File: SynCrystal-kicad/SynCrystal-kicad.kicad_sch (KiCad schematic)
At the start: 34 parts, among them Q1 BC847, SW1 SW_Push, SW2 SW_Push, U1 NCS20071, U2 74HC14, U3 MCP4725, U4 LMC6482, U5 LMC6482, U6 FSA3157L6X

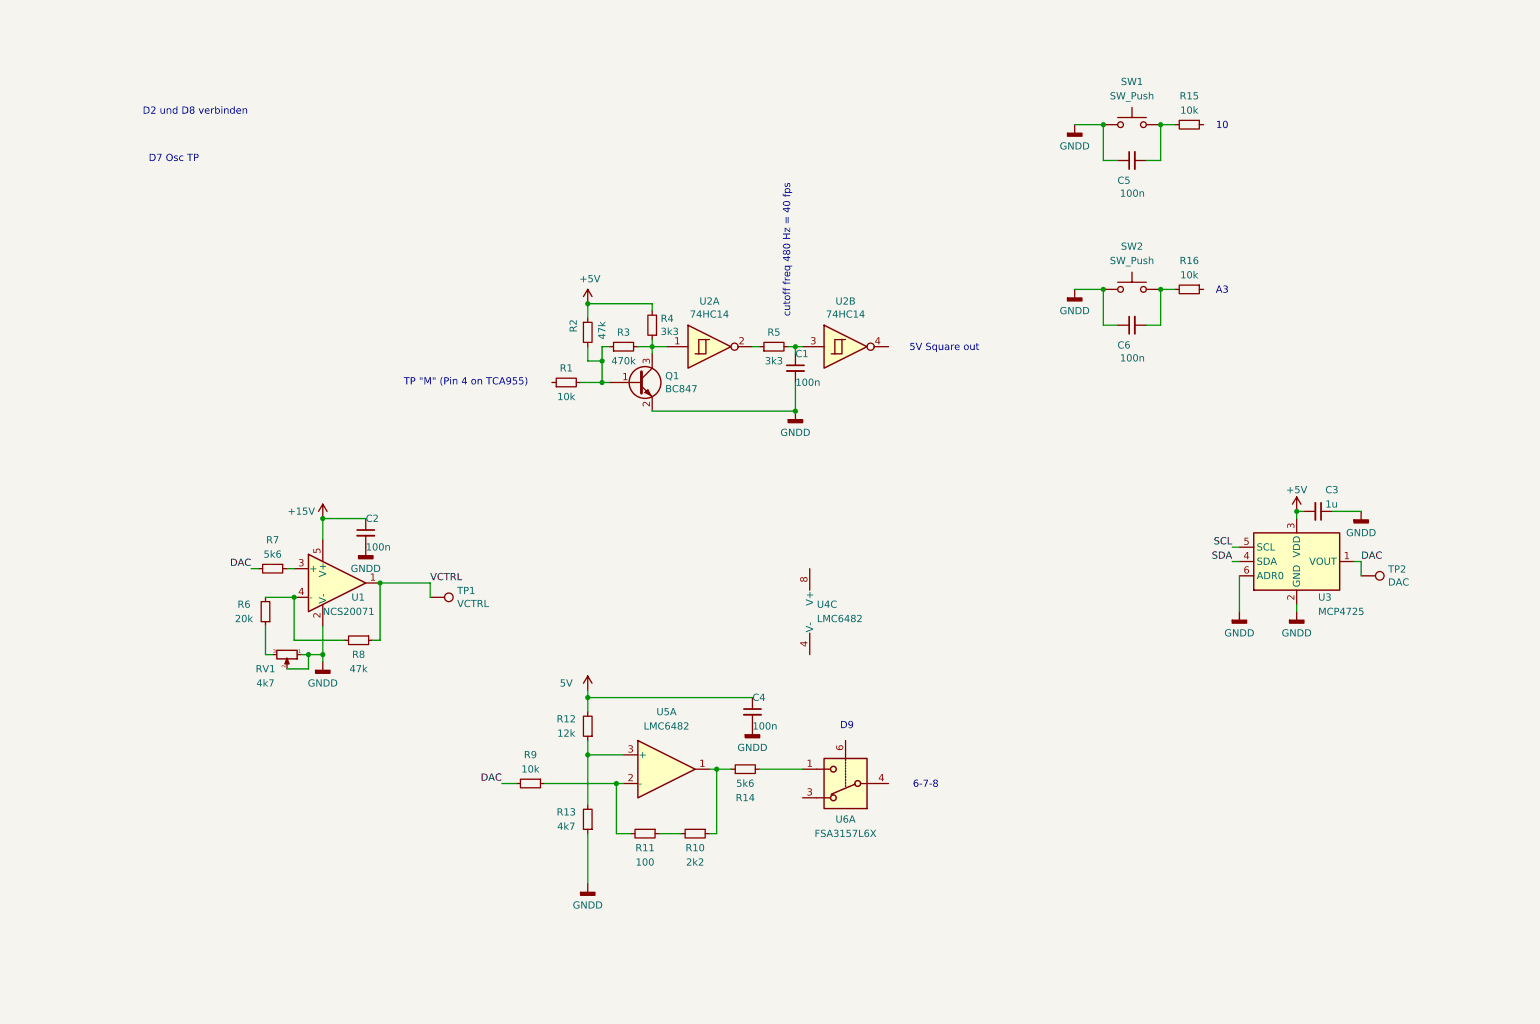
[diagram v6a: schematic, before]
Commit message: pulling the schamtice together
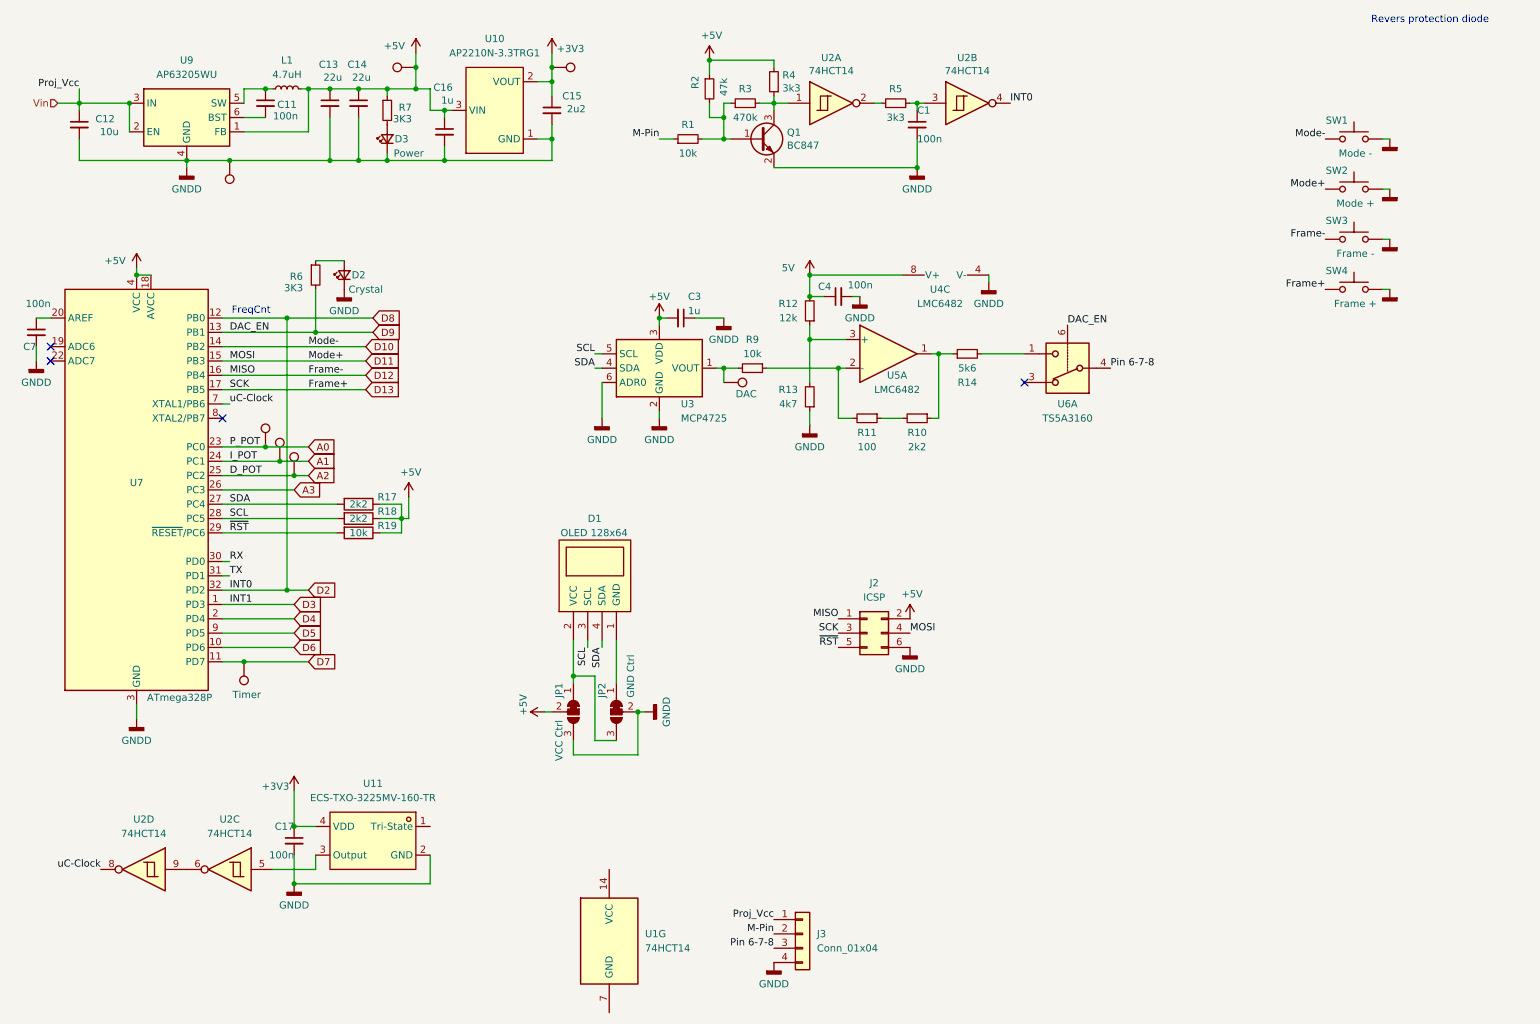
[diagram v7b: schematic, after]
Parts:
- removed C2, C5, C6: 100n, Capacitor_SMD:C_0805_2012Metric, symbol Device:C_Small
- removed R15, R16: 10k, Resistor_SMD:R_0805_2012Metric, symbol Device:R_Small
- removed R8: 47k, Resistor_SMD:R_0805_2012Metric, symbol Device:R_Small
- removed RV1: 4k7, Potentiometer_THT:Potentiometer_Bourns_3296W_Vertical, symbol Device:R_POT_Small
- removed TP1: VCTRL, TestPoint:TestPoint_THTPad_1.5x1.5mm_Drill0.7mm, symbol Connector:TestPoint
- removed TP2: DAC, TestPoint:TestPoint_THTPad_1.5x1.5mm_Drill0.7mm, symbol Connector:TestPoint
- removed U1: NCS20071, Package_TO_SOT_SMD:TSOT-23-5, symbol ErnoCCC-rescue:NCS20071-Amplifier_Operational
- added C11, C17, C7: 100n, Capacitor_SMD:C_0805_2012Metric, symbol Device:C_Small
- added C12: 10u, Capacitor_SMD:C_0805_2012Metric, symbol Device:C_Small
- added C13, C14: 22u, Capacitor_SMD:C_0805_2012Metric, symbol Device:C_Small
- added C15: 2u2, Capacitor_SMD:C_0805_2012Metric, symbol Device:C_Small
- added C16: 1u, Capacitor_SMD:C_0805_2012Metric, symbol Device:C_Small
- added D1: OLED 128x64, Connector_PinHeader_2.54mm:PinHeader_1x04_P2.54mm_Horizontal_shorter, symbol Peacemans Teile:OLED-128-64-I2C-Display_Character
- added D2: Crystal, LED_SMD:LED_0805_2012Metric, symbol Device:LED_Small
- added D3: Power, LED_SMD:LED_0805_2012Metric, symbol Device:LED_Small
- added J2: ICSP, symbol Connector_Generic:Conn_02x03_Odd_Even
- added J3: Conn_01x04, symbol Connector_Generic:Conn_01x04
- added JP1: VCC Ctrl, Jumper:SolderJumper-3_P1.3mm_Bridged12_RoundedPad1.0x1.5mm, symbol Jumper:SolderJumper_3_Bridged12
- added JP2: GND Ctrl, Jumper:SolderJumper-3_P1.3mm_Bridged12_RoundedPad1.0x1.5mm, symbol Jumper:SolderJumper_3_Bridged12
- added L1: 4.7uH, symbol Device:L_Small
- added R17, R18: 2k2, Resistor_SMD:R_0805_2012Metric, symbol Device:R
- added R19: 10k, Resistor_SMD:R_0805_2012Metric, symbol Device:R
- added SW3: Frame -, symbol Switch:SW_Push
- added SW4: Frame +, symbol Switch:SW_Push
- added TP1: P, Peacemans_Footprints:TestPoint_THTPad_1.5x1.5mm_Drill0.7mm_named, symbol Peacemans Teile:TestPoint_named
- added TP2: DAC, Peacemans_Footprints:TestPoint_THTPad_1.5x1.5mm_Drill0.7mm_named, symbol Peacemans Teile:TestPoint_named
- added TP3: I, Peacemans_Footprints:TestPoint_THTPad_1.5x1.5mm_Drill0.7mm_named, symbol Peacemans Teile:TestPoint_named
- added TP4: Timer, Peacemans_Footprints:TestPoint_THTPad_1.5x1.5mm_Drill0.7mm_named, symbol Peacemans Teile:TestPoint_named
- added TP5: D, Peacemans_Footprints:TestPoint_THTPad_1.5x1.5mm_Drill0.7mm_named, symbol Peacemans Teile:TestPoint_named
- added TP6: 5V, Peacemans_Footprints:TestPoint_THTPad_1.5x1.5mm_Drill0.7mm_named, symbol Peacemans Teile:TestPoint_named
- added TP7: 3V3, Peacemans_Footprints:TestPoint_THTPad_1.5x1.5mm_Drill0.7mm_named, symbol Peacemans Teile:TestPoint_named
- added TP8: GND, Peacemans_Footprints:TestPoint_THTPad_1.5x1.5mm_Drill0.7mm_named, symbol Peacemans Teile:TestPoint_named
- added U1: 74HCT14, symbol Peacemans Teile:74HCT14
- added U10: AP2210N-3.3TRG1, easyeda2kicad:SOT-23-3_L2.9-W1.3-P1.90-LS2.4-BR, symbol easyEDA:AP2210N-3.3TRG1
- added U11: ECS-TXO-3225MV-160-TR, easyeda2kicad:OSC-SMD_4P-L3.2-W2.5-BL, symbol easyEDA:ECS-TXO-3225MV-160-TR
- added unit 3 of U2
- added unit 4 of U2
- added U7: ATmega328P, Package_QFP:TQFP-32_7x7mm_P0.8mm, symbol MCU_Microchip_ATmega:ATmega328P-AU
- added U9: AP63205WU, Package_TO_SOT_SMD:TSOT-23-6, symbol Regulator_Switching:AP63205WU
- R6: value 20k -> 3K3; Inventory (none) -> B; LCSC (none) -> C26010
- R7: value 5k6 -> 3K3; Inventory (none) -> B; LCSC (none) -> C26010
- SW1: value SW_Push -> Mode -
- SW2: value SW_Push -> Mode +
- U2: value 74HC14 -> 74HCT14; symbol 74xx:74HC14 -> Peacemans Teile:74HCT14
- U6: value FSA3157L6X -> TS5A3160
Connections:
- net +5V: now also R7.1, C13.1, C14.1, C16.1, J2.2 (Pin_2), JP1.2 (C), L1.2, R17.1, R18.1, R19.1, TP6.1, U10.3 (VIN), U7.18 (AVCC), U7.4 (VCC), U7.6 (VCC), U9.1 (FB)
- net 5V: now also U4.8 (V+)
- net GNDD: now also U4.4 (V-), C12.2, C13.2, C14.2, C15.2, C16.2, C17.2, C7.2, D2.1 (K), D3.1 (K), J2.6 (Pin_6), J3.4 (Pin_4), JP1.3 (B), JP2.2 (C), SW3.1, SW4.1, TP8.1, U10.1 (GND), U11.2 (GND), U7.21 (GND), U7.3 (GND), U7.5 (GND), U9.4 (GND)
- net SCL: now also D1.3 (SCL), R18.2, U7.28 (PC5)
- net SDA: now also D1.4 (SDA), R17.2, U7.27 (PC4)
- net D10: now reaches SW1.2
- net D10: now also U7.14 (PB2)
- net D9: now reaches R6.2
- net D9: now also U6.6, U7.13 (PB1)
- net M-Pin: now reaches R1.1
- net M-Pin: now also J3.2 (Pin_2)
- net at R6.1: now also D2.2 (A)
- net D11: now reaches SW2.2
- net D11: now also J2.4 (Pin_4), U7.15 (PB3)
- net D2: now reaches U2.4
- net D2: now also U7.12 (PB0), U7.32 (PD2)
- net Pin 6-7-8: now reaches U6.4
- net Pin 6-7-8: now also J3.3 (Pin_3)
- net DAC: no longer names the net of R9.2, U3.1 (VOUT)
- net DAC: now also TP2.1; no longer R7.2
- new net: C11.1, L1.1, U9.5 (SW)
- new net: C11.2, U9.6 (BST)
- new net: U11.3 (Output), U2.5
- new net: U2.6, U2.9
- new net: D3.2 (A), R7.2
- new net: C7.1, U7.20 (AREF)
- new net: D1.2 (VCC), JP1.1 (A), JP2.3 (B)
- new net: D1.1 (GND), JP2.1 (A)
- new net +3V3: C15.1, C17.1, TP7.1, U10.2 (VOUT), U11.4 (VDD)
- new net A0: TP1.1, U7.23 (PC0)
- new net A1: TP3.1, U7.24 (PC1)
- new net A2: TP5.1, U7.25 (PC2)
- new net A3: U7.26 (PC3)
- new net D12: J2.1 (Pin_1), SW3.2, U7.16 (PB4)
- new net D13: J2.3 (Pin_3), SW4.2, U7.17 (PB5)
- new net D3: U7.1 (PD3)
- new net D4: U7.2 (PD4)
- new net D5: U7.9 (PD5)
- new net D6: U7.10 (PD6)
- new net D7: TP4.1, U7.11 (PD7)
- new net RX: U7.30 (PD0)
- new net TX: U7.31 (PD1)
- new net Vin: C12.1, J3.1 (Pin_1), U9.2 (EN), U9.3 (IN)
- new net uC-Clock: U2.8, U7.7 (XTAL1/PB6)
- new net ~{RST}: J2.5 (Pin_5), R19.2, U7.29 (~{RESET}/PC6)
- no-connect marks 0 -> 4
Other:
- note added: "FreqCnt"
- note added: "Revers protection diode"
- note removed: "10"
- note removed: "5V Square out"
- note removed: "6-7-8"
- note removed: "A3"
- note removed: "D2 und D8 verbinden"
- note removed: "D7 Osc TP"
- note removed: "D9"
- note removed: "TP "M" (Pin 4 on TCA955)"
- note removed: "cutoff freq 480 Hz = 40 fps"
- moved on the sheet: C1, C3, C4, Q1, R1, R10, R11, R12, R13, R14, R2, R3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

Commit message: Schematics Progress
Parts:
- added C11, C12: 100n, Capacitor_SMD:C_0805_2012Metric, symbol Device:C_Small
- added C13: 330n, Capacitor_SMD:C_0805_2012Metric, symbol Device:C_Small
- added D3, D6: 1N5819, symbol Device:D_Schottky_Small
- added D5: Ext. Imp., LED_SMD:LED_0805_2012Metric, symbol Device:LED_Small
- added D7: in sync, LED_SMD:LED_0805_2012Metric, symbol Device:LED_Small
- added Q2: BC847, Package_TO_SOT_SMD:SOT-23, symbol Transistor_BJT:BC847
- added R17: 1k, Resistor_SMD:R_0805_2012Metric, symbol Device:R_Small
- added R18, R19: 10k, Resistor_SMD:R_0805_2012Metric, symbol Device:R_Small
- added R20, R21: 100k, Resistor_SMD:R_0805_2012Metric, symbol Device:R_Small
- added R22: 100K, Resistor_SMD:R_0805_2012Metric, symbol Device:R_Small
- added R23: 47, Resistor_SMD:R_0805_2012Metric, symbol Device:R_Small
- added R24: 3K3, Resistor_SMD:R_0805_2012Metric, symbol Device:R_Small
- added RV1: 10k, symbol Device:R_Potentiometer_Small
- added TP10, TP8: Ext. Imp., Peacemans_Footprints:TestPoint_THTPad_1.5x1.5mm_Drill0.7mm_named, symbol Peacemans Teile:TestPoint_named
- added unit 5 of U1
- added unit 2 of U4
- J2: renamed from J3; value Conn_01x04 -> Projector
- TP9: renamed from TP4; value Timer -> Pulse Out
- renumbered C11 to C1, C7 to C10, C17 to C14, C13 to C2, C14 to C3, C15 to C4, C12 to C5, C1 to C6, C16 to C7, C4 to C8, C3 to C9, D3 to D1, D1 to D4, J2 to J1, R4 to R1, R9 to R10, R13 to R11, R11 to R12, R10 to R13, R17 to R14, R18 to R15, R19 to R16, R5 to R4, R7 to R5, R1 to R6, R6 to R7, R12 to R8, R14 to R9, TP6 to TP1, TP7 to TP2, TP8 to TP3, TP2 to TP4, TP1 to TP5, TP3 to TP6, TP5 to TP7, U2 to U1, U10 to U2, U9 to U3, U5 to U4, U3 to U5, U11 to U8
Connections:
- net 5V: now also D3.1 (K)
- net D3: now also C12.2, TP10.1, U1.10
- net D5: now also R24.1
- net GNDD: now also C13.1, D5.1 (K), D6.2 (A), D7.1 (K), Q2.2 (E), R20.1, R21.1, R22.2, R23.2
- new net: D5.2 (A), R17.1
- new net: C13.2, R19.1, U1.11
- new net: C11.1, D3.2 (A), D6.1 (K), R18.1, R20.2
- new net: R18.2, TP8.1
- new net: R19.2, RV1.3, U4.7
- new net: C11.2, R21.2, U4.5 (+)
- new net: C12.1, Q2.1 (B), R22.1
- new net: R23.1, RV1.1
- new net: RV1.2, U4.6 (-)
- new net: D7.2 (A), R24.2
- new net: Q2.3 (C), R17.2
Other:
- note added: "Revers protection diode Dumb Mode w/o Display"
- note added: "Works with 1000 Hz Bursts as well as square waves from 3-99% duty cylce"
- note removed: "Revers protection diode"
- moved on the sheet: C8, C9, J1, R10, R11, R12, R13, R8, R9, U1G, U4A, U4C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
